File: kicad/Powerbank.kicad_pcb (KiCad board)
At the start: 4 copper layers, 90 x 60 mm, 167 parts, among them IC1 BQ4050RSMR, IC2 SN74LVC1G14DSFR, IC3 SN74LVC1G08DSFR, IC4 BQ25703ARSNT, IC5 TPD6S300ARUKR, IC6 W25Q80DVSNIG, J1 USB_C_Receptacle, J2 USB_A, J3 Conn_01x02_Male, J4 Conn_01x05_Male, J5 Conn_01x08_Male, J6 Conn_01x04_Male, Q1 Q_NMOS_GDS, Q2 Q_PMOS_GDS, Q3 Q_NMOS_GDS, Q4 Q_NMOS_GDS, Q5 Q_NMOS_GDS, Q6 Q_NMOS_GDS, Q7 Q_NMOS_GDS, Q8 Q_PMOS_GDS, SW1 SW_DIP_x01, U1 TPS65988DH

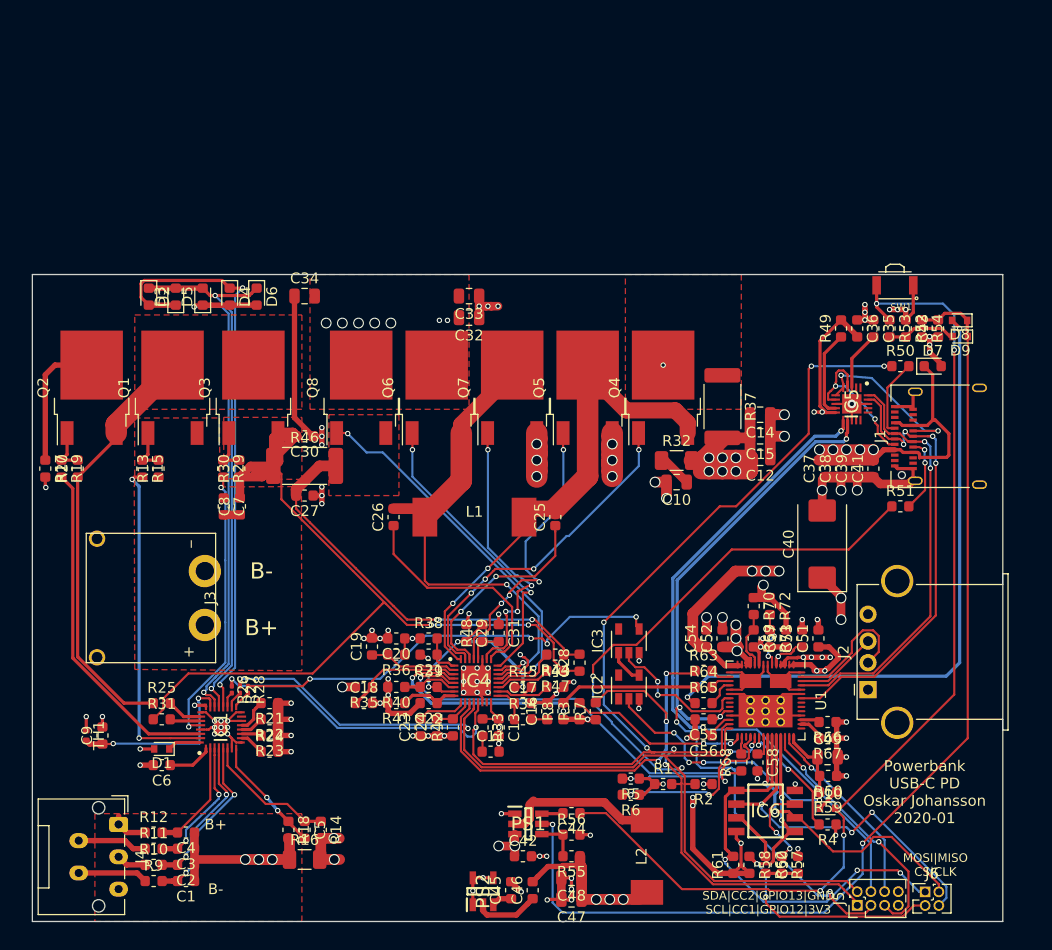
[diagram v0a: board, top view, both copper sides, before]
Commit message: Updated schematic
Made some error with first rev, the found error are now corrected.
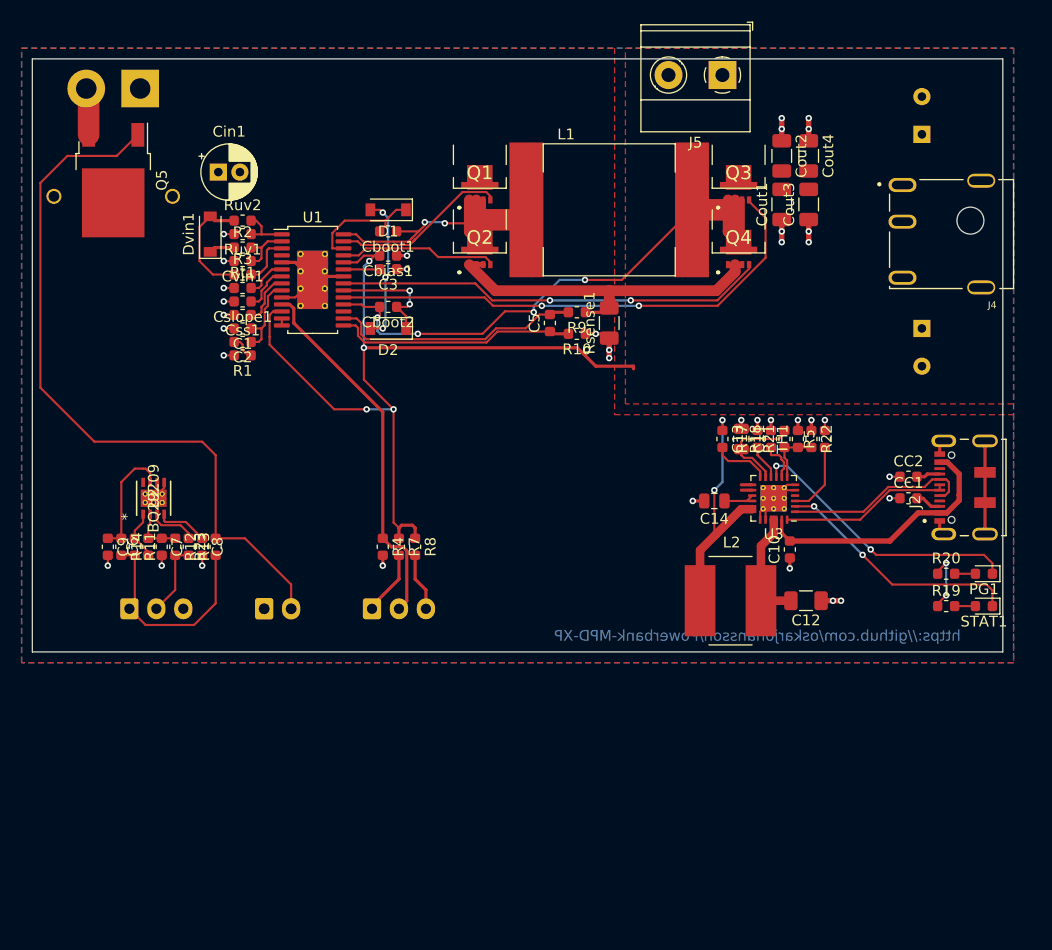
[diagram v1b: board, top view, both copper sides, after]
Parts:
- removed C15, C32, C33, C34, C47, C48, C49: 22µF, Capacitor_SMD:C_0805_2012Metric
- removed C16: 680pF, Capacitor_SMD:C_0603_1608Metric
- removed C17: 15pF, Capacitor_SMD:C_0603_1608Metric
- removed C18, C19: 0.033µF, Capacitor_SMD:C_0603_1608Metric
- removed C20, C37, C38, C39, C41: 0.01µF, Capacitor_SMD:C_0603_1608Metric
- removed C21: 0.47µF, Capacitor_SMD:C_0603_1608Metric
- removed C22, C23, C24: 100pF, Capacitor_SMD:C_0603_1608Metric
- removed C25, C26: 0.047µF, Capacitor_SMD:C_0603_1608Metric
- removed C27, C29, C36, C45, C54: 1µF, Capacitor_SMD:C_0603_1608Metric
- removed C28, C35, C4, C44, C46, C50: 0.1µF, Capacitor_SMD:C_0603_1608Metric
- removed C30, C42, C43, C51, C52, C53, C57: 10µF, Capacitor_SMD:C_0603_1608Metric
- removed C31: 2.2µF, Capacitor_SMD:C_0603_1608Metric
- removed C40: 100µF, Capacitor_Tantalum_SMD:CP_EIA-7343-15_Kemet-W
- removed C55, C56: 330pF, Capacitor_SMD:C_0603_1608Metric
- removed C58: 4.7µF, Capacitor_SMD:C_0603_1608Metric
- removed D10, D8, D9: D_Schottky, Diode_SMD:D_SOD-523
- removed D3, D4, D5, D6: LED, LED_SMD:LED_0603_1608Metric
- removed D7: D_Schottky, Diode_SMD:D_0603_1608Metric
- removed IC1: BQ4050RSMR, Powerbank:QFN40P400X400X100-33N-D
- removed IC2: SN74LVC1G14DSFR, Package_TO_SOT_SMD:SOT-23-5
- removed IC3: SN74LVC1G08DSFR, Package_TO_SOT_SMD:SOT-23-5
- removed IC4: BQ25703ARSNT, Powerbank:QFN40P400X400X80-33N-D
- removed IC5: TPD6S300ARUKR, Powerbank:QFN40P300X300X80-21N-D
- removed IC6: W25Q80DVSNIG, Powerbank:SOIC127P600X175-8N
- removed J6: Conn_01x04_Male, Connector_PinHeader_1.27mm:PinHeader_2x02_P1.27mm_Vertical
- removed PS1: TPS563200DDCT, Powerbank:SOT95P280X110-6N
- removed PS2: TLV70433DBVR, Powerbank:SOT95P280X145-5N
- removed Q6, Q7: Q_NMOS_GDS, Package_TO_SOT_SMD:TO-252-2
- removed Q8: Q_PMOS_GDS, Package_TO_SOT_SMD:TO-252-2
- removed R15, R29: 5.1k, Resistor_SMD:R_0603_1608Metric
- removed R16: 0.001, Resistor_SMD:R_1206_3216Metric
- removed R24, R31, R34, R56, R71: 10k, Resistor_SMD:R_0603_1608Metric
- removed R25: 100R, Resistor_SMD:R_0603_1608Metric
- removed R26, R27, R28: DNP, Resistor_SMD:R_0201_0603Metric
- removed R30: 10M, Resistor_SMD:R_0603_1608Metric
- removed R32: 2.2R, Resistor_SMD:R_1206_3216Metric
- removed R33: 40.2k, Resistor_SMD:R_0603_1608Metric
- removed R35, R36: 4.99R, Resistor_SMD:R_0603_1608Metric
- removed R37, R46: 0.01R, Resistor_SMD:R_2512_6332Metric
- removed R38: 1R, Resistor_SMD:R_0603_1608Metric
- removed R39, R40: 100K, Resistor_SMD:R_0603_1608Metric
- removed R41: 137k, Resistor_SMD:R_0603_1608Metric
- removed R42: 30k, Resistor_SMD:R_0603_1608Metric
- removed R43, R49, R54, R60, R67, R69, R70, R72: 100k, Resistor_SMD:R_0603_1608Metric
- removed R44, R47, R48: 10R, Resistor_SMD:R_0603_1608Metric
- removed R45: 35k, Resistor_SMD:R_0603_1608Metric
- removed R50, R51: DNP, Resistor_SMD:R_0603_1608Metric
- removed R52, R53, R59: 270k, Resistor_SMD:R_0603_1608Metric
- removed R55: 54.9k, Resistor_SMD:R_0603_1608Metric
- removed R57, R58, R61, R62: 3.3k, Resistor_SMD:R_0603_1608Metric
- removed R6: 3.83k, Resistor_SMD:R_0603_1608Metric
- removed R63, R64, R65, R68: 0, Resistor_SMD:R_0603_1608Metric
- removed R66: 5.10k, Resistor_SMD:R_0603_1608Metric
- added CC1: 5.1k, Resistor_SMD:R_0603_1608Metric, F.Cu at (181.2, 90.8)
- added CC2: 5.1k, Resistor_SMD:R_0603_1608Metric, F.Cu at (181.2, 88.8)
- added Cbias1: 0.1uF, Capacitor_SMD:C_0603_1608Metric, F.Cu at (133.0, 68.2)
- added Cboot1: 0.1uF, Capacitor_SMD:C_0603_1608Metric, F.Cu at (133.0, 66.0)
- added Cboot2: 0.1uF, Capacitor_SMD:C_0603_1608Metric, F.Cu at (133.0, 73.0)
- added Cin1: 68uF, Capacitor_THT:CP_Radial_D5.0mm_P2.00mm, F.Cu at (117.2, 60.5)
- added Cout1: 10uF, Capacitor_SMD:C_1206_3216Metric, F.Cu at (169.5, 63.5)
- added Cout2: 10uF, Capacitor_SMD:C_1206_3216Metric, F.Cu at (169.5, 59.0)
- added Cout3: 10uF, Capacitor_SMD:C_1206_3216Metric, F.Cu at (172.0, 63.5)
- added Cout4: 10uF, Capacitor_SMD:C_1206_3216Metric, F.Cu at (172.0, 59.0)
- added Cout5: 180uF, Capacitor_THT:CP_Radial_D8.0mm_P3.50mm, B.Cu at (182.5, 57.0)
- added Cout6: 180uF, Capacitor_THT:CP_Radial_D8.0mm_P3.50mm, B.Cu at (182.5, 75.0)
- added Cslope1: 220pF, Capacitor_SMD:C_0603_1608Metric, F.Cu at (119.5, 72.5)
- added Css1: 0.1uF, Capacitor_SMD:C_0603_1608Metric, F.Cu at (119.5, 73.8)
- added Cvin1: 0.1uF, Capacitor_SMD:C_0603_1608Metric, F.Cu at (119.5, 68.8)
- added Dvin1: VIN, Diode_SMD:D_SOD-123, F.Cu at (116.5, 66.2)
- added PG1: ~PG, Diode_SMD:D_0603_1608Metric, F.Cu at (188.2, 97.8)
- added Rsense1: R008, Resistor_SMD:R_1206_3216Metric, F.Cu at (153.5, 74.5)
- added Rt1: 27.4k, Resistor_SMD:R_0603_1608Metric, F.Cu at (119.5, 71.2)
- added Ruv1: 59k, Resistor_SMD:R_0603_1608Metric, F.Cu at (119.5, 66.2)
- added Ruv2: 249k, Resistor_SMD:R_0603_1608Metric, F.Cu at (119.5, 65.0)
- added STAT1: STAT, Diode_SMD:D_0603_1608Metric, F.Cu at (188.2, 100.8)
- added SW2: Select_Vout, Connector_JST:JST_XH_B3B-XH-A_1x03_P2.50mm_Vertical, B.Cu at (131.5, 101.0)
- added U2: BQ29209, outdoor-sense-footprint:BQ29209DRBR, F.Cu at (111.2, 90.8)
- added U3: BQ25886, Package_DFN_QFN:VQFN-24-1EP_4x4mm_P0.5mm_EP2.45x2.45mm_ThermalVias, F.Cu at (168.8, 90.8)
- C1: value 0.1µF -> 560pF
- C10: value 22µF -> 1uF; footprint Capacitor_SMD:C_0805_2012Metric -> Capacitor_SMD:C_0603_1608Metric
- C11: value 1800pF -> 4.7uF; footprint Capacitor_SMD:C_0603_1608Metric -> Capacitor_SMD:C_0805_2012Metric
- C12: value 22µF -> 10uF; footprint Capacitor_SMD:C_0805_2012Metric -> Capacitor_SMD:C_1206_3216Metric
- C13: value 33pF -> 47nF
- C14: value 22µF -> 4.7uF
- C2: value 0.1µF -> 33nF
- C3: value 0.1µF -> 1uF
- C5: value 0.1µF -> 47pF
- C6: value 2.2µF -> 0.1uF
- C7, C9: value 0.1µF -> 0.1uF
- C8: value 0.22µF -> 0.1uF
- D1: value D_Schottky -> Dboot1; footprint Diode_SMD:D_SOD-523 -> Diode_SMD:D_SOD-123
- D2: value LED -> Dboot2; footprint LED_SMD:LED_0603_1608Metric -> Diode_SMD:D_SOD-123
- J1: value USB_C_Receptacle -> Balance conn; footprint Connector_USB:USB_C_Receptacle_Amphenol_12401610E4-2A -> Connector_JST:JST_XH_B3B-XH-A_1x03_P2.50mm_Vertical; moved to B.Cu
- J2: value USB_A -> USB_C_Receptacle_USB2.0; footprint Connector_USB:USB_A_Stewart_SS-52100-001_Horizontal -> connectors:USB_C_JAE_DX07S016JA1R1500
- J3: value Conn_01x02_Male -> Bat conn; footprint Powerbank:XT30PW-M -> connectors:XT30PW-M; moved to B.Cu
- J4: value Conn_01x05_Male -> Barrel_jack; footprint Connector_JST:JST_ZE_S05B-ZESK-2D_1x05_P1.50mm_Horizontal -> connectors:PJ079BH
- J5: value Conn_01x08_Male -> OUT; footprint Connector_PinHeader_1.27mm:PinHeader_2x04_P1.27mm_Vertical -> connectors:TerminalBlock_02_P5.00mm
- L1: value 2.2µH -> 4.7uH; footprint Powerbank:WE_Inductor_7443330220 -> inductor:Pulse_PA4344.XXXNLT
- L2: value 3.3µH -> 1uH; footprint Powerbank:WE_Inductor_8070_7443340330 -> Inductor_SMD:L_Bourns_SRN8040TA
- Q1, Q3, Q4: value Q_NMOS_GDS -> NVTFS5C466NL; footprint Package_TO_SOT_SMD:TO-252-2 -> mosfet:8-PowerWDFN
- Q2: value Q_PMOS_GDS -> NVTFS5C466NL; footprint Package_TO_SOT_SMD:TO-252-2 -> mosfet:8-PowerWDFN
- Q5: value Q_NMOS_GDS -> Q_PMOS_GDS
- R1: value 3.83k -> 10k
- R10, R9: value 100R -> 100
- R11: value 100R -> 160
- R12: value 100R -> 260
- R13: value 10M -> 100
- R17: value 300 -> 5.7k
- R18: value 100 -> 383
- R19: value 5.1k -> 1k
- R2: value 3.83k -> 10
- R20: value 10M -> 1k
- R21: value 10k -> 5.23k
- R22: value 10k -> 30.1k
- R3: value 10k -> 2k
- R4: value 10k -> 20k
- R5: value 3.83k -> 0
- R7: value 3.83k -> 280k
- R8: value 3.83k -> 580k
- SW1: value SW_DIP_x01 -> ON/OFF; footprint Powerbank:SW_B3U-3000P -> Connector_JST:JST_XH_B2B-XH-A_1x02_P2.50mm_Vertical; moved to B.Cu
- TH1: footprint Resistor_SMD:R_0402_1005Metric -> Resistor_SMD:R_0603_1608Metric
- U1: value TPS65988DH -> LM34936-Q1; footprint Powerbank:QFN-56_7x7_Pitch0.4mm -> Package_SO:HTSSOP-28-1EP_4.4x9.7mm_P0.65mm_EP2.85x5.4mm_ThermalVias
- moved J4 100.1 mm to (191.0, 65.0), turned to 180 degrees
- moved R19 83.0 mm to (184.8, 100.8), turned to 0 degrees
- moved R20 81.1 mm to (184.8, 97.8), turned to 0 degrees
- moved J5 78.0 mm to (164.0, 51.5), turned to 180 degrees
- moved J1 77.7 mm to (109.0, 101.0), turned to 0 degrees
- moved TH1 71.5 mm to (171.0, 85.2), turned to 90 degrees
- moved R17 66.1 mm to (167.2, 85.2), turned to 90 degrees
- moved R9 65.8 mm to (150.5, 73.5), turned to 180 degrees
- moved SW1 65.7 mm to (121.5, 101.0), turned to 0 degrees
- moved R2 65.6 mm to (119.5, 67.5), turned to 0 degrees
- moved R10 63.0 mm to (150.5, 75.5), turned to 180 degrees
- moved R18 57.6 mm to (168.5, 85.2), turned to 90 degrees
- moved U1 57.3 mm to (126.0, 70.5), turned to 0 degrees
- moved C3 56.9 mm to (133.0, 69.5)
- moved R22 56.6 mm to (172.2, 85.2), turned to 270 degrees
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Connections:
- C1 pad 1: -BATT -> /Boost module/COMP
- C1 pad 2: Net-(C1-Pad2) -> GND
- C10 pad 1: Net-(C10-Pad1) -> GND
- C10 pad 2: GND -> /Charge module/VBUS
- C11 pad 1: Net-(C11-Pad1) -> GND
- C11 pad 2: GND -> /Charge module/REGN
- C12 pad 2: PP_HV -> /Charge module/PMID
- C13 pad 1: COMP1 -> /Charge module/SW
- C13 pad 2: GND -> Net-(C13-Pad2)
- C14 pad 1: GND -> Net-(C14-Pad1)
- C14 pad 2: PP_HV -> GND
- C2 pad 1: -BATT -> /Boost module/COMP
- C3 pad 1: -BATT -> GND
- C3 pad 2: Net-(C3-Pad2) -> /Boost module/VCC
- C6 pad 2: -BATT -> Net-(C6-Pad2)
- C7 pad 1: CELL4 -> Net-(C6-Pad2)
- C7 pad 2: Net-(C7-Pad2) -> GND
- C8 pad 1: Net-(C7-Pad2) -> Net-(C8-Pad1)
- C8 pad 2: +VDC -> GND
- C9 pad 2: CELL4 -> GND
- D1 pad 1: Net-(D1-Pad1) -> Net-(Cboot1-Pad2)
- D1 pad 2: CELL4 -> /Boost module/VCC
- D2 pad 1: Net-(D2-Pad1) -> Net-(Cboot2-Pad1)
- D2 pad 2: Net-(D2-Pad2) -> /Boost module/VCC
- J3 pad 1: CELL4 -> GND
- J3 pad 2: -BATT -> /Battery/CELL2
- J4 pad 1: CELL4 -> /Boost module/VOUT
- J4 pad 2: CELL3 -> GND
- J4 pad 3: CELL2 -> GND
- J5 pad 1: SCL_1 -> /Boost module/VOUT
- J5 pad 2: SDA_1 -> GND
- L1 pad 1: TP1 -> Net-(Cboot1-Pad1)
- L1 pad 2: TP2 -> Net-(Cboot2-Pad2)
- L2 pad 1: Net-(L2-Pad1) -> /Charge module/SW
- L2 pad 2: +5V -> /Charge module/PMID
- Q1 pad 1: Net-(Q1-Pad1) -> Net-(Cboot1-Pad1)
- Q1 pad 2: /Cell Balancer BQ4050/Source -> Net-(Q1-Pad2)
- Q1 pad 3: CELL4 -> +VDC
- Q2 pad 3: /Cell Balancer BQ4050/Source -> Net-(Cboot1-Pad1)
- Q3 pad 1: Net-(Q3-Pad1) -> Net-(Cboot2-Pad2)
- Q3 pad 2: /Cell Balancer BQ4050/Source -> Net-(Q3-Pad2)
- Q3 pad 3: +VDC -> /Boost module/VOUT
- Q4 pad 1: TP5 -> Net-(Q2-Pad1)
- Q4 pad 2: Net-(C20-Pad1) -> Net-(Q4-Pad2)
- Q4 pad 3: TP1 -> Net-(Cboot2-Pad2)
- Q5 pad 1: TP3 -> Net-(Q5-Pad1)
- Q5 pad 2: TP1 -> +VDC
- Q5 pad 3: GND -> /Battery/CELL2
- R1 pad 1: PD_LDO_3V3 -> Net-(C2-Pad2)
- R1 pad 2: SCL_1 -> GND
- R10 pad 1: CELL2 -> GND
- R10 pad 2: Net-(C2-Pad2) -> Net-(C5-Pad1)
- R11 pad 1: CELL3 -> Net-(C6-Pad1)
- R11 pad 2: Net-(C3-Pad2) -> /Battery/CELL2
- R12 pad 1: CELL4 -> Net-(C6-Pad2)
- R12 pad 2: Net-(C4-Pad2) -> /Battery/CELL1
- R13 pad 1: CELL4 -> Net-(R13-Pad1)
- R13 pad 2: Net-(Q1-Pad1) -> /Battery/CELL1
- R14 pad 1: Net-(C5-Pad1) -> Net-(C9-Pad1)
- R14 pad 2: GND -> /Battery/CELL2
- R17 pad 1: Net-(Q2-Pad2) -> /Charge module/ICHGSET
- R17 pad 2: CELL4 -> GND
- R18 pad 1: Net-(C5-Pad2) -> /Charge module/ILIM
- R18 pad 2: -BATT -> GND
- R19 pad 1: Net-(Q2-Pad1) -> +VDC
- R2 pad 1: PD_LDO_3V3 -> Net-(Dvin1-Pad1)
- R2 pad 2: SDA_1 -> Net-(Cvin1-Pad1)
- R20 pad 1: /Cell Balancer BQ4050/Source -> +VDC
- R20 pad 2: Net-(Q2-Pad1) -> Net-(PG1-Pad2)
- R21 pad 1: -BATT -> Net-(R21-Pad1)
- R21 pad 2: Net-(IC1-Pad13) -> /Charge module/REGN
- R22 pad 1: -BATT -> GND
- R22 pad 2: Net-(IC1-Pad12) -> Net-(R21-Pad1)
- R23 pad 1: -BATT -> /Battery/CELL2
- R23 pad 2: Net-(IC1-Pad11) -> Net-(Q5-Pad1)
- R3 pad 1: PD_LDO_3V3 -> +VDC
- R3 pad 2: IRQ_1 -> Net-(R3-Pad2)
- R4 pad 1: PD_LDO_3V3 -> /Boost module/FB
- R4 pad 2: IRQ_2 -> GND
- R5 pad 1: PD_LDO_3V3 -> /Charge module/~CE
- R5 pad 2: SCL_2 -> GND
- R7 pad 1: PD_LDO_3V3 -> /Boost module/VOUT
- R7 pad 2: PROCHOT -> Net-(R7-Pad2)
- R8 pad 1: PD_LDO_3V3 -> /Boost module/VOUT
- R8 pad 2: CHRG_OK -> Net-(R8-Pad2)
- R9 pad 1: CELL1 -> Net-(Q2-Pad1)
- R9 pad 2: Net-(C1-Pad2) -> Net-(C5-Pad2)
- SW1 pad 1: SYS -> GND
- SW1 pad 2: SW -> Net-(Q5-Pad1)
- TH1 pad 1: CELL4 -> Net-(R21-Pad1)
- TH1 pad 2: Net-(C9-Pad1) -> GND
- U1 pad 1: +5V -> Net-(Ruv1-Pad1)
- U1 pad 10: ADCIN2 -> GND
- U1 pad 11: PP_HV -> /Boost module/FB
- U1 pad 12: PP_HV -> /Boost module/VOUT
- U1 pad 13: VBUS_C -> GND
- U1 pad 14: VBUS_C -> GND
- U1 pad 15: DRAIN1 -> Net-(C5-Pad1)
- U1 pad 16: Net-(R63-Pad2) -> Net-(C5-Pad2)
- U1 pad 18: Net-(R65-Pad2) -> Net-(Cboot2-Pad2)
- U1 pad 19: DRAIN1 -> Net-(Q3-Pad2)
- U1 pad 2: +5V -> Net-(Cvin1-Pad1)
- U1 pad 20: GND -> Net-(Cboot2-Pad1)
- U1 pad 21: SNK_EVENT -> Net-(Q4-Pad2)
- U1 pad 22: SRC_EVENT_LED -> GND
- U1 pad 23: TP12 -> /Boost module/VCC
- U1 pad 24: CC1 -> /Boost module/VOUT
- U1 pad 25: GND -> Net-(Q2-Pad2)
- U1 pad 26: CC2 -> Net-(Cboot1-Pad2)
- U1 pad 27: SCL_1 -> Net-(Q1-Pad2)
- U1 pad 28: SDA_1 -> Net-(Cboot1-Pad1)
- U1 pad 29: IRQ_1 -> GND
- U1 pad 3: VBUS_A -> Net-(R3-Pad2)
- U1 pad 4: VBUS_A -> MODE
- U1 pad 5: +3V3 -> GND
- U1 pad 6: ADCIN1 -> /Boost module/RTSYNC
- U1 pad 7: DRAIN2 -> Net-(Cslope1-Pad1)
- U1 pad 8: DRAIN1 -> Net-(Css1-Pad1)
- U1 pad 9: PD_LDO_3V3 -> /Boost module/COMP
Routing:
- net SYS: track 145.2 -> 0.00 mm, vias 13 -> 0
- net SCL_1: track 143.2 -> 0.00 mm, vias 8 -> 0
- net SDA_1: track 134.7 -> 0.00 mm, vias 4 -> 0
- net PD_LDO_3V3: track 117.0 -> 0.00 mm, vias 11 -> 0
- net SYS_EN: track 99.0 -> 0.00 mm, vias 2 -> 0
- net SW: track 96.1 -> 0.00 mm, vias 4 -> 0
- net PP_HV: track 94.9 -> 0.00 mm, vias 10 -> 0
- net GND: track 156.5 -> 72.1 mm, vias 82 -> 36
- net /Boost module/VOUT: track 0.00 -> 78.7 mm, vias 0 -> 4
- net CC1: track 73.7 -> 0.00 mm, vias 5 -> 0
- net VBUS_C: track 72.8 -> 0.00 mm, vias 8 -> 0
- net +3V3: track 72.5 -> 0.00 mm, vias 2 -> 0
- net +VDC: track 88.9 -> 18.4 mm
- net Net-(Q5-Pad1): track 0.00 -> 67.5 mm
- net CC2: track 66.2 -> 0.00 mm, vias 2 -> 0
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- added copper zone on F.Cu, net /Boost module/VOUT
- added copper zone on B.Cu, net GND
- removed copper zone on F.Cu, net -BATT
- removed copper zone on GND.Cu, net -BATT
- removed copper zone on F.Cu, net /Cell Balancer BQ4050/Source
- removed copper zone on F.Cu, net CELL4
- removed copper zone on POWER.Cu, net CELL4
- removed copper zone on GND.Cu, net GND
- removed copper zone on F.Cu, net Net-(C20-Pad1)
- removed copper zone on F.Cu, net Net-(C27-Pad2)
- removed copper zone on F.Cu, net SYS
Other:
- board size 90 x 60 mm -> 90 x 55 mm
- copper layers 4 -> 2
- net class Default: via_dia 0.5 -> 0.6
- rule trace_min: 0.1 -> 0.2
- rule via_min_size: 0.5 -> 0.6
- board text added: "12V/24V"
- board text added: "2S Li-ion"
- board text added: "B-|BM|B+"
- board text added: "ON/OFF"
- board text added: "Powerbank for MPD XP & TS100 Rev 1 - 20201204"
- board text added: "https://github.com/oskarjohansson/Powerbank-MPD-XP"
- board text removed: "B+"
- board text removed: "B-"
- board text removed: "MOSI|MISO CS|CLK"
- board text removed: "Powerbank USB-C PD Oskar Johansson 2020-01"
- board text removed: "SDA|CC2|GPIO13|GND SCL|CC1|GPIO12|3V3"
